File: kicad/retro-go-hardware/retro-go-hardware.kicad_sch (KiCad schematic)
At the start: 7 parts

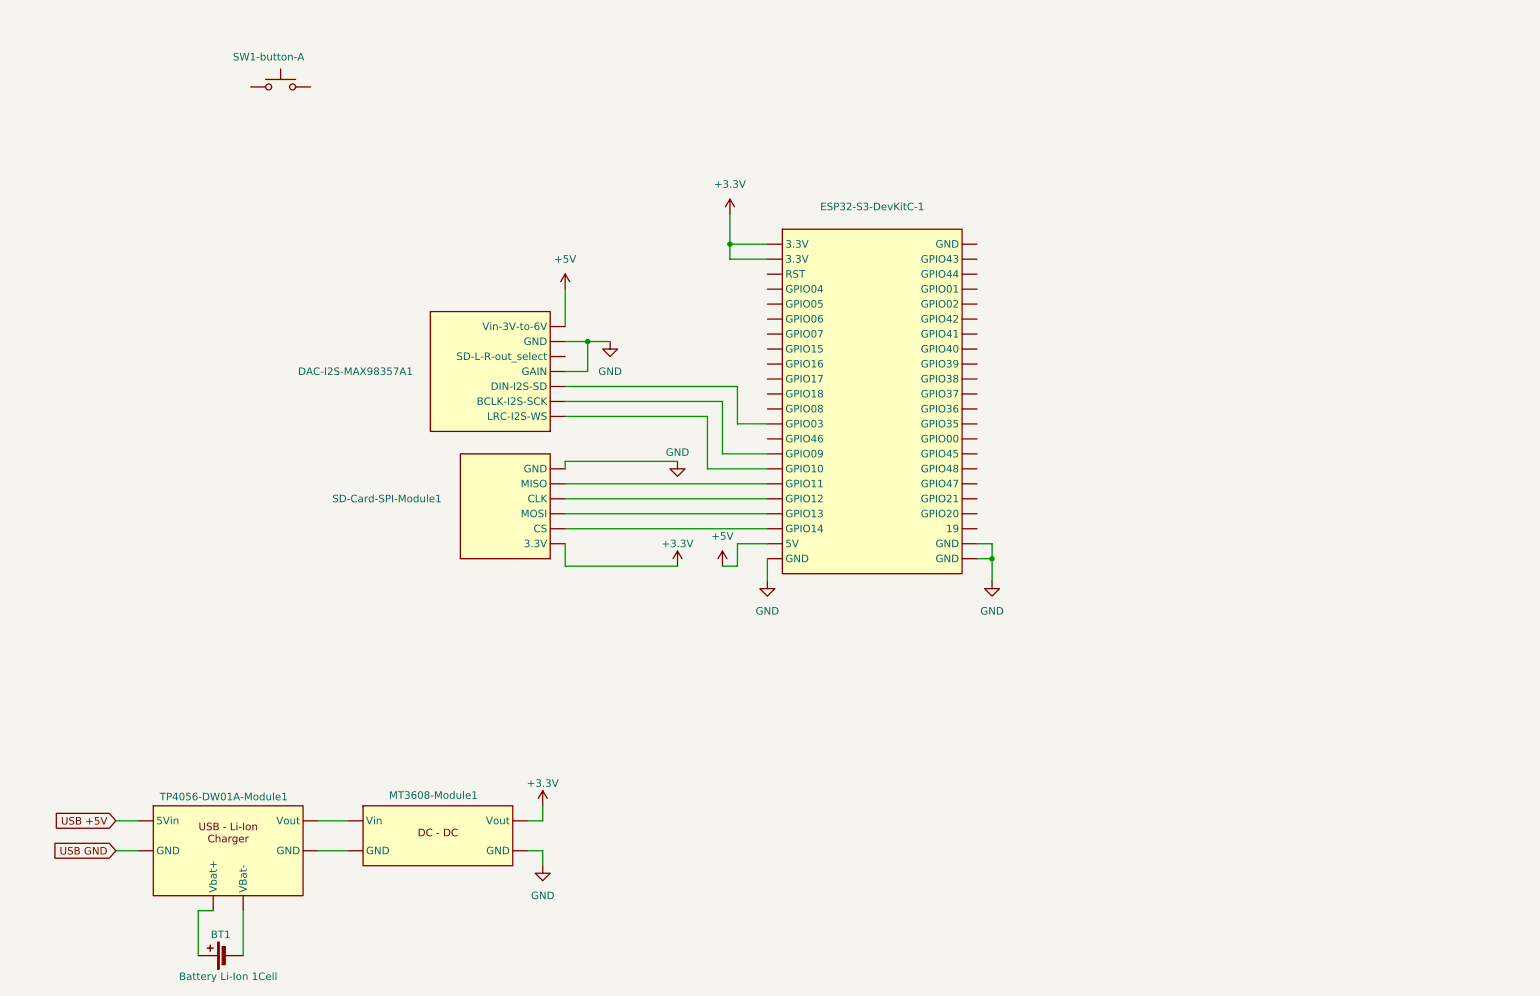
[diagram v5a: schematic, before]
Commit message: Fixed component in library, added speaker
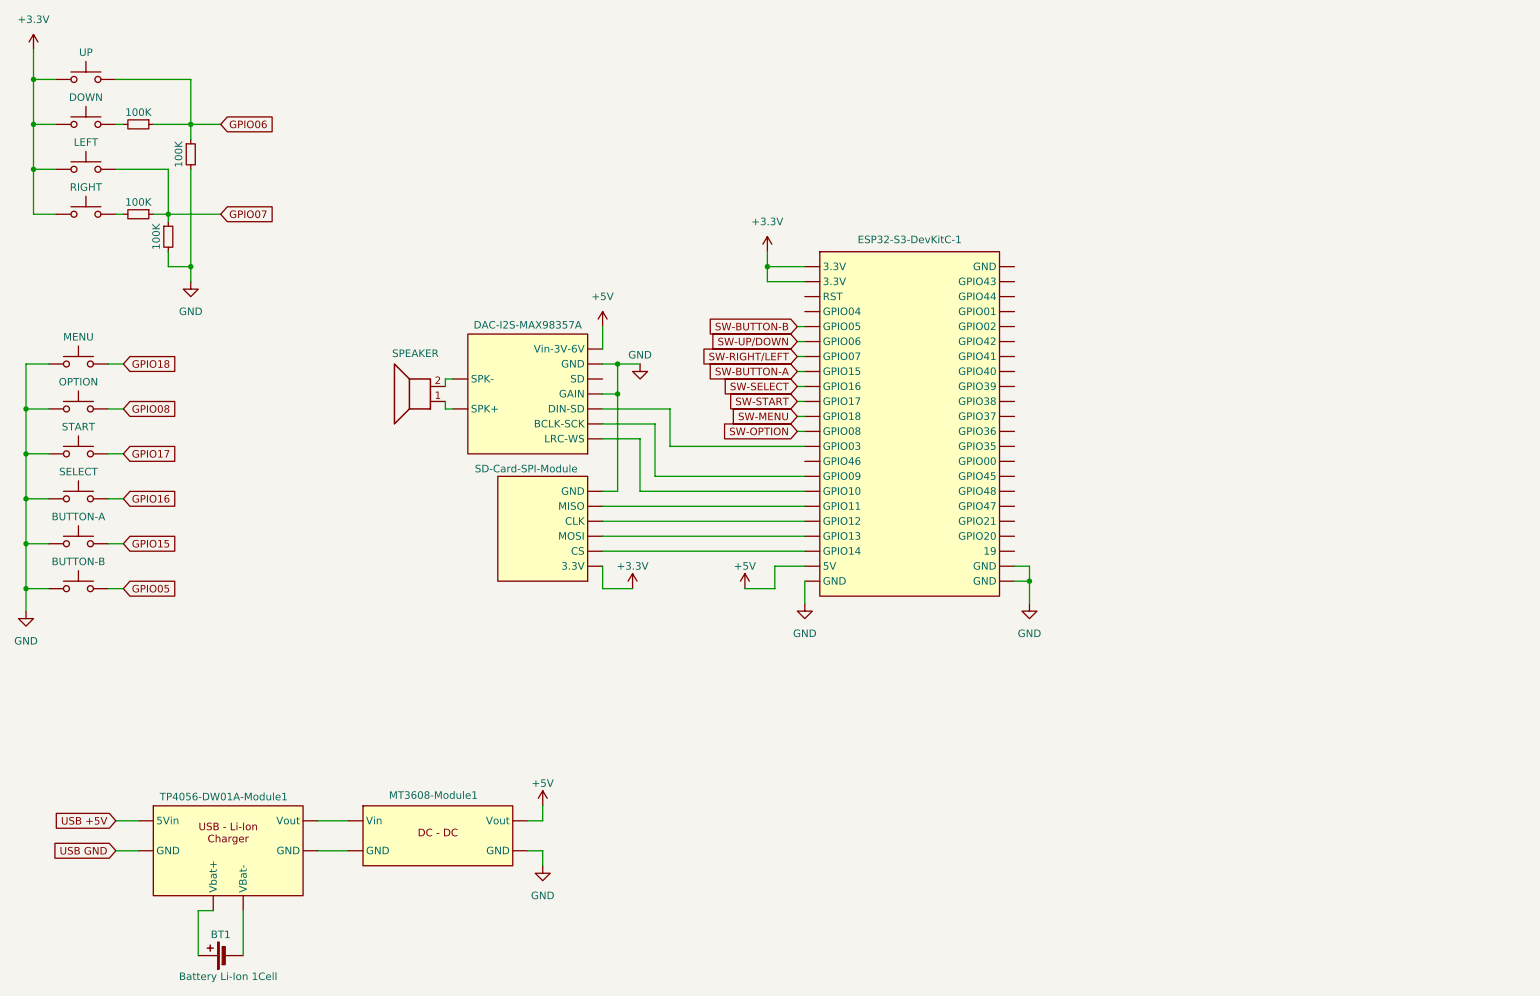
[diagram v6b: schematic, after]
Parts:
- removed DAC-I2S-MAX98357A1: ~, symbol CustomLibrary:DAC-I2S-MAX98357A
- added BUTTON-A, BUTTON-B, DOWN, LEFT, MENU, OPTION, RIGHT, SELECT, START: ~, symbol Switch:SW_Push
- added DAC-I2S-MAX98357A: ~, symbol CustomLibrary:DAC-I2S-MAX98357A
- added R1, R2, R3, R4: 100K, symbol Device:R_Small
- added SPEAKER: Speaker, symbol Device:Speaker
- renumbered SD-Card-SPI-Module1 to SD-Card-SPI-Module, SW1-button-A to UP
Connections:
- net +3.3V: now also UP.1, DOWN.1, LEFT.1, RIGHT.1; no longer MT3608-Module1. (Vout)
- net +5V: now also MT3608-Module1. (Vout), DAC-I2S-MAX98357A. (Vin-3V-6V)
- net GND: now also BUTTON-A.1, BUTTON-B.1, DAC-I2S-MAX98357A. (Vin-3V-6V), MENU.1, OPTION.1, R3.2, R4.2, SELECT.1, START.1
- net GPIO06: now reaches UP.2
- net GPIO06: now also R1.1, R3.1
- net SW-UP/DOWN: now reaches ESP32-S3-DevKitC-1. (RST)
- net SW-UP/DOWN: no longer SD-Card-SPI-Module. (MOSI)
- new net: DAC-I2S-MAX98357A. (Vin-3V-6V), ESP32-S3-DevKitC-1. (RST) (x3)
- new net: DAC-I2S-MAX98357A. (Vin-3V-6V), SPEAKER.1
- new net: DAC-I2S-MAX98357A. (Vin-3V-6V), SPEAKER.2
- new net: R2.2, RIGHT.2
- new net: ESP32-S3-DevKitC-1. (RST), SD-Card-SPI-Module. (MOSI) (x4)
- new net: DOWN.2, R1.2
- new net: MT3608-Module1. (Vout), TP4056-DW01A-Module1. (Vout) (x2)
- new net GPIO05: BUTTON-B.2
- new net GPIO07: LEFT.2, R2.1, R4.1
- new net GPIO08: OPTION.2
- new net GPIO15: BUTTON-A.2
- new net GPIO16: SELECT.2
- new net GPIO17: START.2
- new net GPIO18: MENU.2
- new net SW-BUTTON-A: ESP32-S3-DevKitC-1. (RST)
- new net SW-BUTTON-B: ESP32-S3-DevKitC-1. (RST)
- new net SW-MENU: ESP32-S3-DevKitC-1. (RST)
- new net SW-OPTION: ESP32-S3-DevKitC-1. (RST)
- new net SW-RIGHT/LEFT: ESP32-S3-DevKitC-1. (RST)
- new net SW-SELECT: ESP32-S3-DevKitC-1. (RST)
- new net SW-START: ESP32-S3-DevKitC-1. (RST)
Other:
- moved on the sheet: ESP32-S3-DevKitC-1, SD-Card-SPI-Module, UP

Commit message: Finishing schematic
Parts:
- added 100n, 100n1, 2.7uF, 2.7uF1: C, symbol Device:C
- added ILI9341: ~, symbol CustomLibrary:ILI9341-Module
- added SW1: ON / OFF Switch, symbol Switch:SW_DPST_x2
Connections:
- net +3.3V: now also 100n.1, ILI9341.2 (GND)
- net +5V: now also 100n1.1, 2.7uF.1, 2.7uF1.1
- net GND: now also 100n.2, 100n1.2, 2.7uF.2, 2.7uF1.2, ILI9341.1 (VCC)
- new net: DAC-I2S-MAX98357A. (Vin-3V-6V), ESP32-S3-DevKitC-1. (RST) (x3)
- new net: ESP32-S3-DevKitC-1. (RST), SD-Card-SPI-Module. (MOSI) (x4)
- new net: SW1.1 (A), TP4056-DW01A-Module1. (Vout)
- new net: MT3608-Module1. (Vout), SW1.2 (B)
- new net: MT3608-Module1. (Vout), TP4056-DW01A-Module1. (Vout)
- new net: ESP32-S3-DevKitC-1. (RST), ILI9341. (RES) (x5)
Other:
- moved on the sheet: MT3608-Module1

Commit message: Added rendered electronic
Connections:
- net at ILI9341. (RES): no longer ESP32-S3-DevKitC-1. (RST)
- new net: DAC-I2S-MAX98357A. (Vin-3V-6V), ESP32-S3-DevKitC-1. (RST) (x3)
- new net: ESP32-S3-DevKitC-1. (RST), SD-Card-SPI-Module. (MOSI) (x4)
- new net: MT3608-Module1. (Vout), TP4056-DW01A-Module1. (Vout)
- new net: ESP32-S3-DevKitC-1. (RST), ILI9341. (RES) (x5)
- now unconnected: ILI9341. (RES), ILI9341. (RES), ILI9341. (RES), ILI9341. (RES)
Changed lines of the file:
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@@
 	(title_block
 		(title "RetroGoHardware")
-		(date "2024-04-09")
-		(rev "0.1")
+		(date "2024-04-18")
+		(rev "1.0")
+		(comment 1 "https://github.com/Akrobate/retro-go-hardware")
 	)
 	(junction
